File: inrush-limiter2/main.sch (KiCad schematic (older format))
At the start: 32 parts, among them K1 RELAY_2RT, P1 CONN_01X04, P2 CONN_01X02, Q1 2N3904, Q2 PN2222A, T1 TRANSFO, U1 LM393, U2 50 ohm NTC

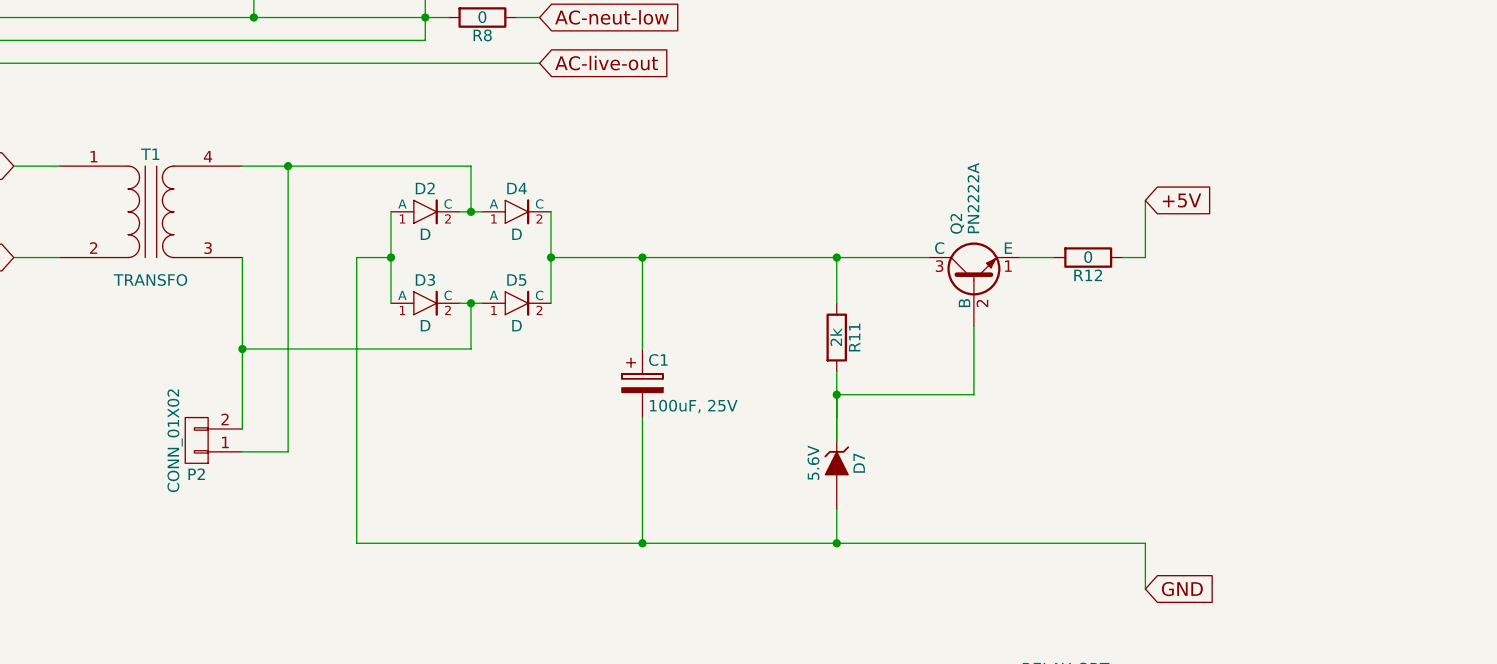
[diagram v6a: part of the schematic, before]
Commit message: add pin headers
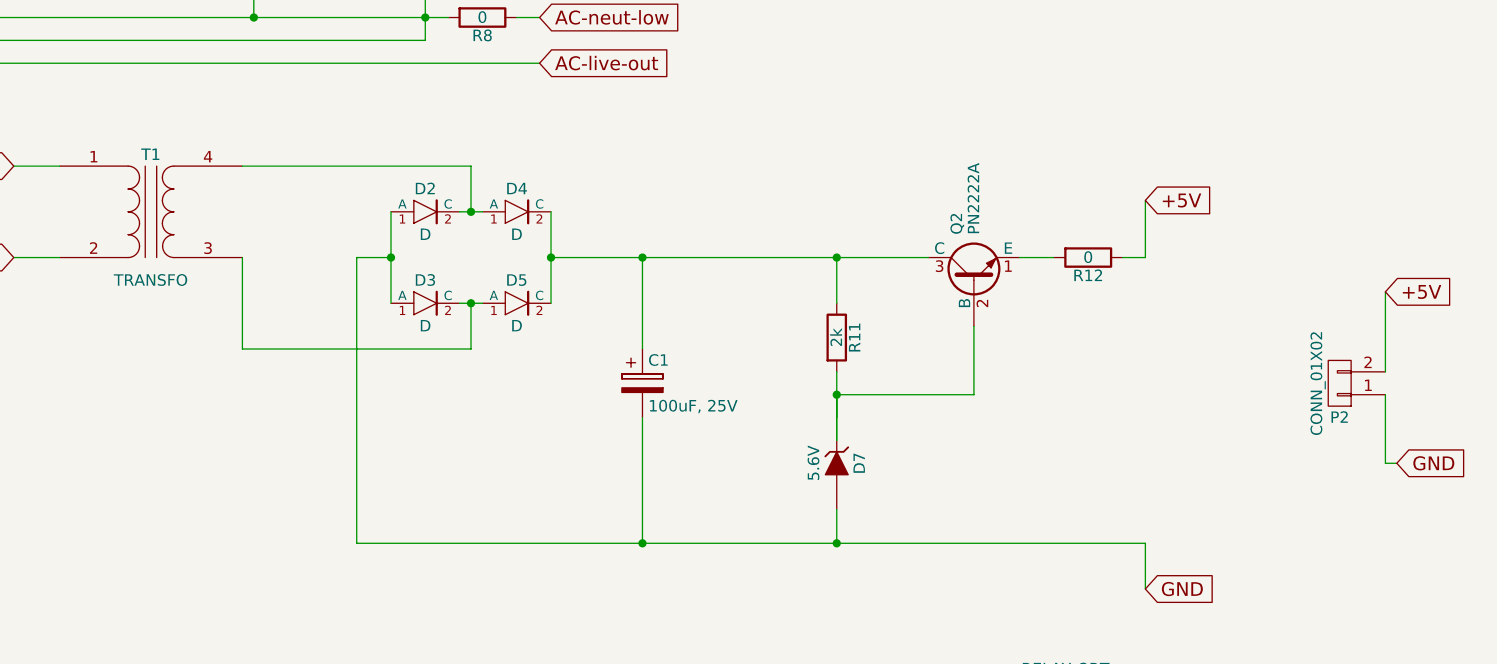
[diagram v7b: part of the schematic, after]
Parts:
- P1: footprint Terminal_Blocks:TerminalBlock_WAGO-804_RM7.5mm_3pol -> test:fuck
- P2: footprint (none) -> Wire_Pads:SolderWirePad_2x_1-2mmDrill
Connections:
- net +5V: now also P2.2 (P2)
- net GND: now also P2.1 (P1)
- net at D2.2 (C), D4.1 (A), T1.4 (SB): no longer P2.1 (P1)
- net at D3.2 (C), D5.1 (A), T1.3 (SA): no longer P2.2 (P2)
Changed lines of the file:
@@
 F 0 "P1" H 1150 1650 50  0000 C CNN
 F 1 "CONN_01X04" V 1250 1400 50  0000 C CNN
-F 2 "Terminal_Blocks:TerminalBlock_WAGO-804_RM7.5mm_3pol" H 1150 1400 50  0001 C CNN
+F 2 "test:fuck" H 1150 1400 50  0001 C CNN
 F 3 "" H 1150 1400 50  0000 C CNN
 	1    1150 1400
@@
 Wire Wire Line
 	1150 4350 5650 4350
-Wire Wire Line
-	2600 2800 3600 2800
 Connection ~ 4350 2400
 Wire Wire Line
@@
 Wire Wire Line
 	3600 2000 3600 2200
-Wire Wire Line
-	2600 2000 3600 2000
 Wire Wire Line
 	3100 3650 6550 3650
@@
 Wire Wire Line
 	2550 4750 2550 4900
+Wire Wire Line
+	2600 2400 2600 2800
 $Comp
 L CONN_01X02 P2
-U 1 1 57CFF614
-P 2400 3200
-F 0 "P2" H 2400 3350 50  0000 C CNN
-F 1 "CONN_01X02" V 2500 3200 50  0000 C CNN
-F 2 "" H 2400 3200 50  0000 C CNN
-F 3 "" H 2400 3200 50  0000 C CNN
-	1    2400 3200
+U 1 1 57D01BCD
+P 7400 2950
+F 0 "P2" H 7400 3100 50  0000 C CNN
+F 1 "CONN_01X02" V 7500 2950 50  0000 C CNN
+F 2 "Wire_Pads:SolderWirePad_2x_1-2mmDrill" H 7400 2950 50  0001 C CNN
+F 3 "" H 7400 2950 50  0000 C CNN
+	1    7400 2950
 	-1   0    0    1
 $EndComp
 Wire Wire Line
-	2600 2400 2600 3150
-Connection ~ 2600 2800
-Wire Wire Line
-	2600 3250 2800 3250
-Wire Wire Line
-	2800 3250 2800 2000
-Connection ~ 2800 2000
+	2600 2000 3600 2000
+Wire Wire Line
+	2600 2800 3600 2800
+Text GLabel 7600 2550 2    60   Input ~ 0
++5V
+Text GLabel 7650 3300 2    60   Input ~ 0
+GND
+Wire Wire Line
+	7600 3000 7600 3300
+Wire Wire Line
+	7600 3300 7650 3300
+Wire Wire Line
+	7600 2900 7600 2550
 $EndSCHEMATC

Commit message: add new transformer schematic and footprint
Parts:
- removed T1: TRANSFO, Transformers_CHK:Trafo_CHK-EI30-2VA_Neutral, symbol TRANSFO
- added T1: MY-TRANSFO, symbol MY-TRANSFO
- P2: footprint Wire_Pads:SolderWirePad_2x_1-2mmDrill -> Pin_Headers:Pin_Header_Straight_1x02
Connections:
- net AC-live-f-low: now also T1.1 (AA)
- net AC-neut-low: now also T1.5 (AB)
- net at D2.2 (C), D4.1 (A): now also T1.9 (SB)
- net at D3.2 (C), D5.1 (A): now also T1.7 (SA)
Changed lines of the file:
@@
-	1    0    0    -1
-$EndComp
-$Comp
-L TRANSFO T1
-U 1 1 57CC83CA
-P 2200 2200
-F 0 "T1" H 2200 2450 50  0000 C CNN
-F 1 "TRANSFO" H 2200 1900 50  0000 C CNN
-F 2 "Transformers_CHK:Trafo_CHK-EI30-2VA_Neutral" H 2200 2200 50  0001 C CNN
-F 3 "" H 2200 2200 50  0000 C CNN
-	1    2200 2200
 	1    0    0    -1
 $EndComp
@@
 	5550 4950 5550 5200
 Wire Wire Line
-	5550 5200 6600 5200
-Wire Wire Line
-	6600 5200 6600 4850
+	6600 5200 5550 5200
+Wire Wire Line
+	6600 4850 6600 5200
 Wire Wire Line
 	6600 4850 6450 4850
@@
 F 0 "P2" H 7400 3100 50  0000 C CNN
 F 1 "CONN_01X02" V 7500 2950 50  0000 C CNN
-F 2 "Wire_Pads:SolderWirePad_2x_1-2mmDrill" H 7400 2950 50  0001 C CNN
+F 2 "Pin_Headers:Pin_Header_Straight_1x02" H 7400 2950 50  0001 C CNN
 F 3 "" H 7400 2950 50  0000 C CNN
 	1    7400 2950
@@
 Wire Wire Line
 	7600 2900 7600 2550
+$Comp
+L MY-TRANSFO T1
+U 1 1 57D04545
+P 2200 2200
+F 0 "T1" H 2200 2450 50  0000 C CNN
+F 1 "MY-TRANSFO" H 2200 1900 50  0000 C CNN
+F 2 "" H 2200 2200 50  0000 C CNN
+F 3 "" H 2200 2200 50  0000 C CNN
+	1    2200 2200
+	1    0    0    -1
+$EndComp
 $EndSCHEMATC
